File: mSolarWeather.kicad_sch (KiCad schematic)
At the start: 27 parts, among them J1 JST2PH Batt LiFePo4, J2 Solar connector, J3 USB C, J4 BME280_I2C, J5 Conn_01x04, J6 Conn_01x04 Stemma QT QW-4MM50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, J7 WIND, J8 RAIN, SW1 SW_Push_Dual, SW2 SW_Push_Dual, U1 BQ29706, U2 TPS63021, U3 ESP32-S3-WROOM-1-N16R2

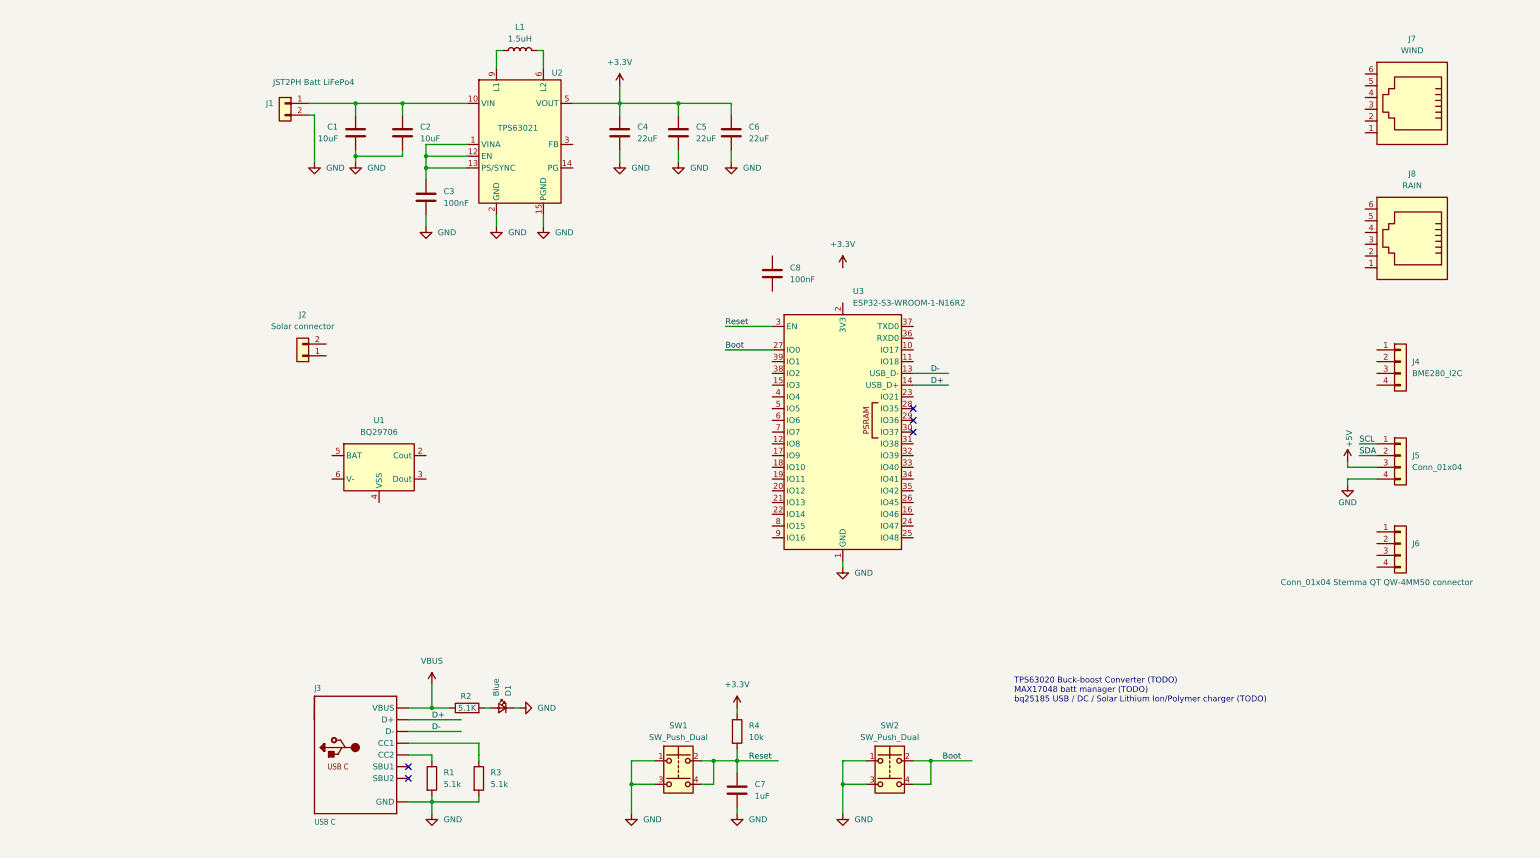
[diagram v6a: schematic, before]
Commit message: update schematic
add SD card
add RTC chip
add Lora module
update BQ25185 configuration for LiFePo4
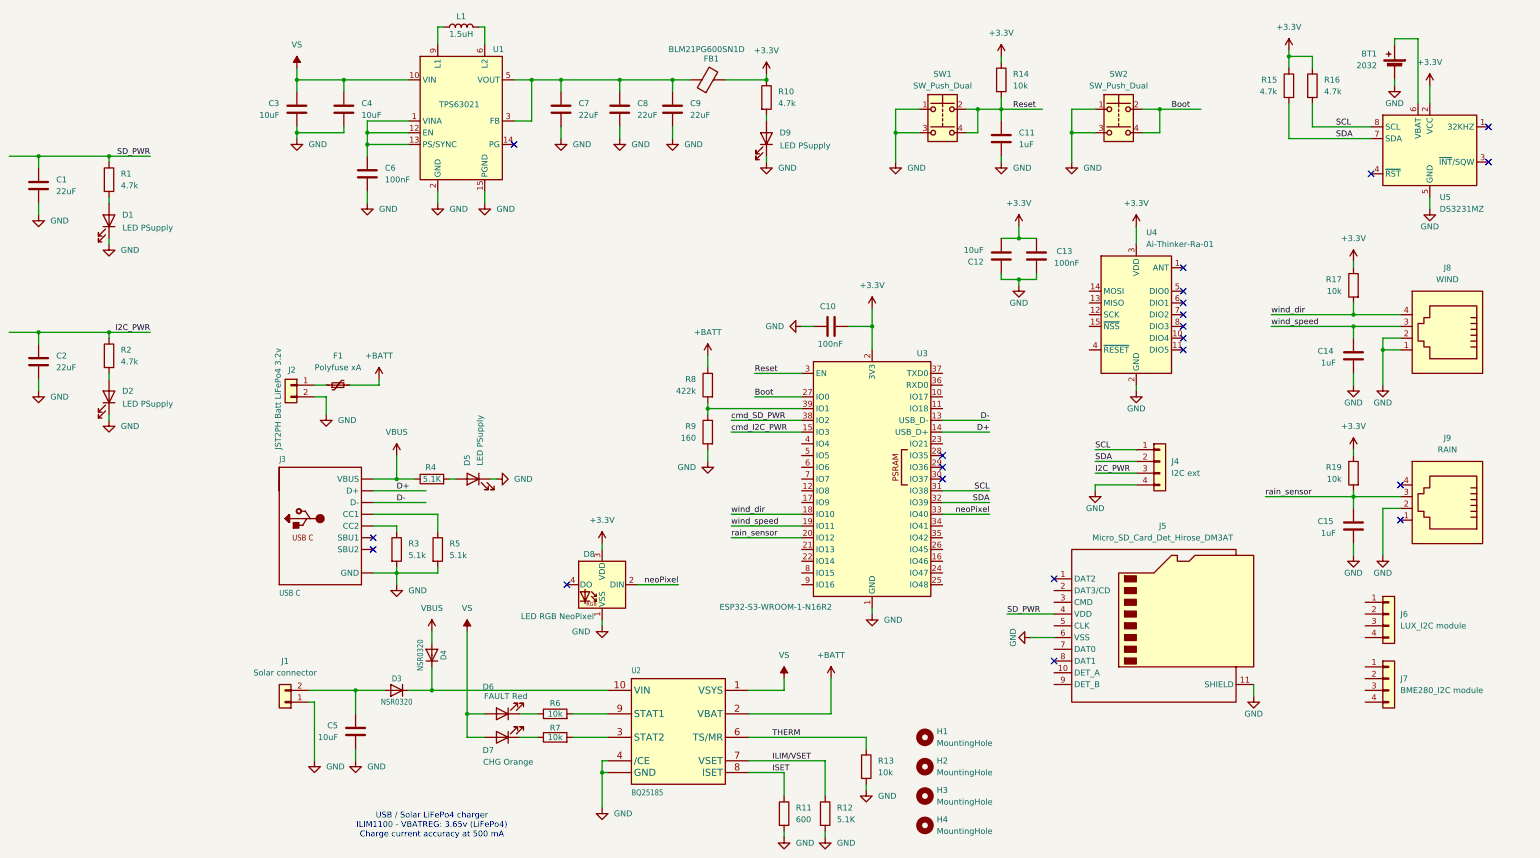
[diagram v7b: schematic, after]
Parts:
- removed D1: Blue, LED_SMD:LED_1206_3216Metric, symbol Device:LED_Small
- removed J7: WIND, Connector_RJ:RJ12_Amphenol_54601-x06_Horizontal, symbol Connector:RJ12
- removed J8: RAIN, Connector_RJ:RJ12_Amphenol_54601-x06_Horizontal, symbol Connector:RJ12
- removed U1: BQ29706, Package_SON:WSON-6_1.5x1.5mm_P0.5mm, symbol Battery_Management:BQ297xy
- removed U2: TPS63021, mSolarLib:VSON_DSJ-14-3x4mm_P0.5mm_ThermalVias, symbol mSolarLib:TPS63021
- added BT1: 2032, Battery:BatteryHolder_MYOUNG_BS-07-A1BJ001_CR2032, symbol Device:Battery_Cell
- added C10, C13: 100nF, Capacitor_SMD:C_0805_2012Metric_Pad1.18x1.45mm_HandSolder, symbol Device:C
- added C12: 10uF, symbol Device:C
- added C14, C15: 1uF, Capacitor_SMD:C_0805_2012Metric_Pad1.18x1.45mm_HandSolder, symbol Device:C
- added C7, C9: 22uF, symbol Device:C
- added D1, D2, D5, D9: LED PSupply, LED_SMD:LED_PLCC-2_3.4x3.0mm_KA, symbol Device:LED
- added D3, D4: NSR0320, Diode_SMD:D_SOD-323_HandSoldering, symbol lifepo4_solar_charger-eagle-import:DIODE_SOD323MINI
- added D6: FAULT Red, LED_SMD:LED_PLCC-2_3.4x3.0mm_KA, symbol Device:LED
- added D7: CHG Orange, LED_SMD:LED_PLCC-2_3.4x3.0mm_KA, symbol Device:LED
- added D8: LED RGB NeoPixel, LED_SMD:LED_Inolux_IN-PI554FCH_PLCC4_5.0x5.0mm_P3.2mm, symbol LED:Inolux_IN-PI554FCH
- added F1: Polyfuse xA, symbol Device:Polyfuse_Small
- added FB1: BLM21PG600SN1D, Inductor_SMD:L_0805_2012Metric_Pad1.15x1.40mm_HandSolder, symbol Device:FerriteBead
- added H1, H2, H3, H4: MountingHole, MountingHole:MountingHole_3.2mm_M3, symbol Mechanical:MountingHole
- added J5: Micro_SD_Card_Det_Hirose_DM3AT, Connector_Card:microSD_HC_Hirose_DM3AT-SF-PEJM5, symbol Connector:Micro_SD_Card_Det_Hirose_DM3AT
- added J8: WIND, Connector_RJ:RJ14_Connfly_DS1133-S4_Horizontal, symbol Connector:RJ14
- added J9: RAIN, Connector_RJ:RJ14_Connfly_DS1133-S4_Horizontal, symbol Connector:RJ14
- added R1, R10, R15, R16, R2: 4.7k, Resistor_SMD:R_0805_2012Metric_Pad1.20x1.40mm_HandSolder, symbol Device:R
- added R11: 600, Resistor_SMD:R_0805_2012Metric_Pad1.20x1.40mm_HandSolder, symbol Device:R
- added R12: 5.1K, Resistor_SMD:R_0805_2012Metric_Pad1.20x1.40mm_HandSolder, symbol Device:R
- added R13, R17, R19, R6, R7: 10k, Resistor_SMD:R_0805_2012Metric_Pad1.20x1.40mm_HandSolder, symbol Device:R
- added R8: 422k, Resistor_SMD:R_0805_2012Metric_Pad1.20x1.40mm_HandSolder, symbol Device:R
- added R9: 160, Resistor_SMD:R_0805_2012Metric_Pad1.20x1.40mm_HandSolder, symbol Device:R
- added U1: TPS63021, mSolarLib:VSON_DSJ-14-3x4mm_P0.5mm_ThermalVias, symbol mSolarLib:TPS63021
- added U2: BQ25185, Package_SON:WSON-10-1EP_2.5x2.5mm_P0.5mm_EP1.2x2mm_ThermalVias, symbol lifepo4_solar_charger-eagle-import:BQ25185
- added U4: Ai-Thinker-Ra-01, RF_Module:Ai-Thinker-Ra-01-LoRa, symbol RF_Module:Ai-Thinker-Ra-01
- added U5: DS3231MZ, Package_SO:SOIC-8_3.9x4.9mm_P1.27mm, symbol Timer_RTC:DS3231MZ
- C1, C2: value 10uF -> 22uF
- C3: value 100nF -> 10uF; footprint Capacitor_SMD:C_0805_2012Metric_Pad1.18x1.45mm_HandSolder -> (none)
- C4, C5: value 22uF -> 10uF
- C6: value 22uF -> 100nF; footprint (none) -> Capacitor_SMD:C_0805_2012Metric_Pad1.18x1.45mm_HandSolder
- C8: value 100nF -> 22uF; footprint Capacitor_SMD:C_0805_2012Metric_Pad1.18x1.45mm_HandSolder -> (none)
- J2: renamed from J1; value JST2PH Batt LiFePo4 -> JST2PH Batt LiFePo4 3.2v
- J3: footprint Adafruit ESP32-S3 Reverse TFT Feather:USB_C_CUSB31-CFM2AX-01-X -> Connector_USB:USB_C_Receptacle_GCT_USB4105-xx-A_16P_TopMnt_Horizontal
- J4: renamed from J5; value Conn_01x04 -> I2C ext
- J6: value Conn_01x04 Stemma QT QW-4MM50 connector -> LUX_I2C module
- J7: renamed from J4; value BME280_I2C -> BME280_I2C module; footprint (none) -> Connector_JST:JST_SH_SM04B-SRSS-TB_1x04-1MP_P1.00mm_Horizontal
- renumbered C7 to C11, J2 to J1, R4 to R14, R1 to R3, R2 to R4, R3 to R5
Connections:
- net +3.3V: now also U3.2 (3V3), C10.2, C12.2, C13.2, D8.3 (VDD), FB1.2, R10.1, R15.1, R16.1, R17.1, R19.1, U4.3 (VDD), U5.2 (VCC); no longer C4.1, C5.1, C6.1
- net GND: now also C8.2, J1.1 (Pin_1), BT1.2 (-), C10.1, C12.1, C13.1, C14.1, C15.1, C7.2, C9.2, D1.1 (K), D2.1 (K), D5.1 (K), D8.1 (VSS), D9.1 (K), J5.11 (SHIELD), J5.6 (VSS), J8.1, J8.2, J9.2, R11.2, R12.2, R13.2, R9.2, U1.15 (PGND), U1.2 (GND), U2.4 (/CE), U2.5 (GND), U2.PAD (GND), U4.16 (GND), U4.2 (GND), U4.9 (GND), U5.5 (GND)
- net SCL: now also U3.31 (IO38), R16.2, U5.8 (SCL)
- net SDA: now also U3.32 (IO39), R15.2, U5.7 (SDA)
- net VBUS: now also D4.A
- net VS: now reaches C3.1
- net VS: now also C4.1, D6.2 (A), D7.2 (A), U1.10 (VIN), U1.11 (VIN), U2.1 (VSYS)
- net at L1.2: now also U1.6 (L2), U1.7 (L2)
- net at L1.1: now also U1.8 (L1), U1.9 (L1)
- net cmd_I2C_PWR: now reaches U3.15 (IO3)
- net wind_dir: now reaches U3.18 (IO10)
- net wind_dir: now also J8.4, R17.2
- net wind_speed: now reaches U3.19 (IO11)
- net wind_speed: now also C14.2, J8.3
- net rain_sensor: now reaches U3.20 (IO12)
- net rain_sensor: now also C15.2, J9.3, R19.2
- net neoPixel: now reaches U3.33 (IO40)
- net neoPixel: now also D8.2 (DIN)
- net cmd_SD_PWR: now reaches U3.38 (IO2)
- net at U3.39 (IO1): now also R8.2, R9.1
- net at R4.2: now also D5.2 (A)
- net at J1.2 (Pin_2): now also C5.1, D3.A
- net at C8.1: now also C7.1, C9.1, FB1.1, U1.3 (FB), U1.4 (VOUT), U1.5 (VOUT)
- net +5V renamed I2C_PWR
- net I2C_PWR: now also C2.1, R2.1
- new net: D6.1 (K), R6.1
- new net: C6.1, U1.1 (VINA), U1.12 (EN), U1.13 (PS/SYNC)
- new net: D2.2 (A), R2.2
- new net: F1.1, J2.1 (Pin_1)
- new net: BT1.1 (+), U5.6 (VBAT)
- new net: D3.C, D4.C, U2.10 (VIN)
- new net: R7.2, U2.3 (STAT2)
- new net: R6.2, U2.9 (STAT1)
- new net: D1.2 (A), R1.2
- new net: D7.1 (K), R7.1
- new net: D9.2 (A), R10.2
- new net +BATT: F1.2, R8.1, U2.2 (VBAT)
- new net ILIM/VSET: R12.1, U2.7 (VSET)
- new net ISET: R11.1, U2.8 (ISET)
- new net SD_PWR: C1.1, J5.4 (VDD), R1.1
- new net THERM: R13.1, U2.6 (TS/MR)
- no-connect marks 5 -> 21
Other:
- note added: "USB / Solar LiFePo4 charger ILIM1100 - VBATREG: 3.65v (LiFePo4) Charge current accuracy at 500 mA"
- note removed: "TPS63020 Buck-boost Converter (TODO) MAX17048 batt manager (TODO) bq25185 USB / DC / Solar Lithium Ion/Polymer charger (TODO)"
- company: cfdev -> Cyril Frausti
- moved on the sheet: C11, J1, J2, J3, J4, J7, L1, R14, R3, R4, R5, SW1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
